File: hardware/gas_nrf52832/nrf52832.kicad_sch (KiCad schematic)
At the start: 15 parts, among them J1 J-link, J4 Conn_01x03, Q3 FDV303N, X1 32.768kHz

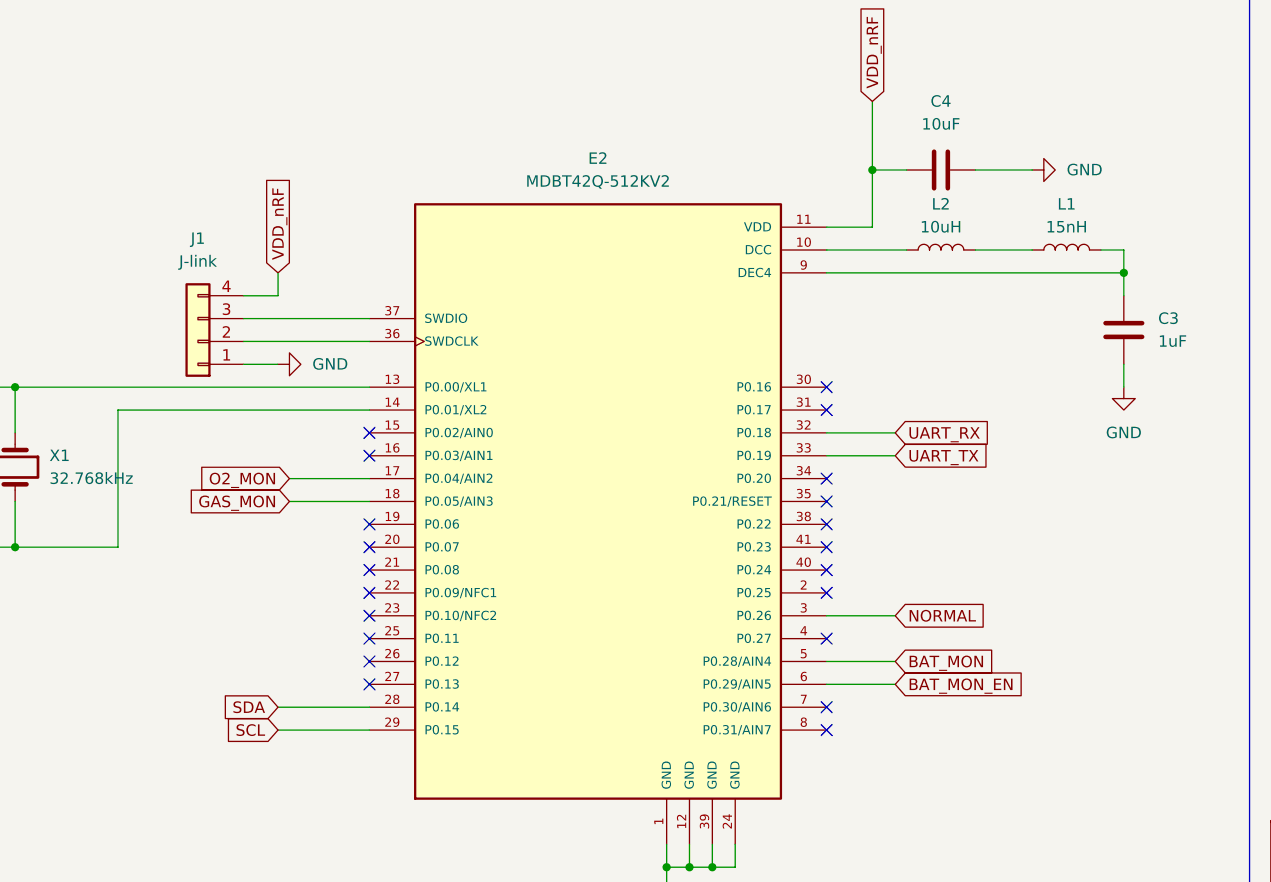
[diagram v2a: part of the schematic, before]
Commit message: test: gas biasing circuit
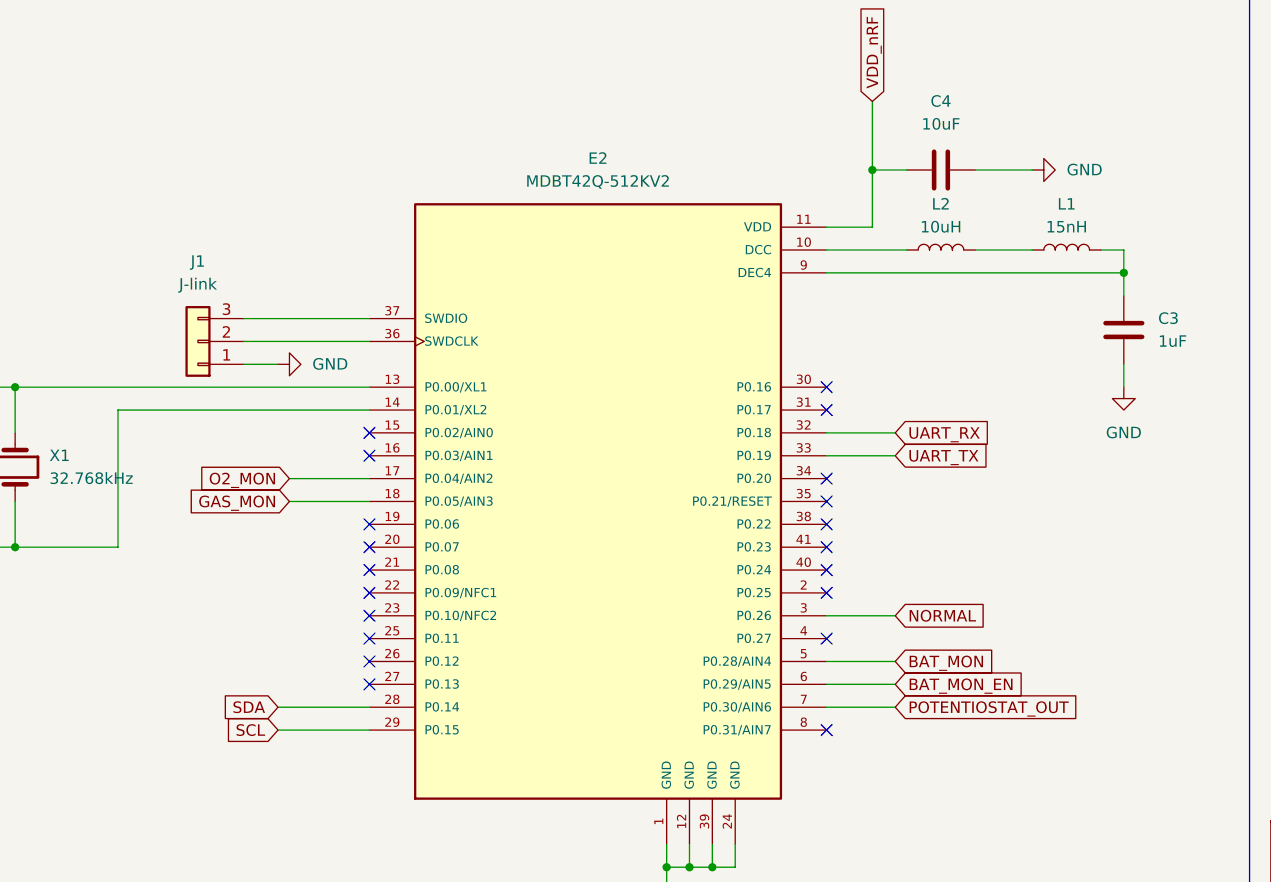
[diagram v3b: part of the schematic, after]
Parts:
- J1: footprint Connector_PinHeader_2.54mm:PinHeader_1x04_P2.54mm_Vertical -> Connector_PinHeader_2.54mm:PinHeader_1x03_P2.54mm_Vertical; symbol Connector_Generic:Conn_01x04 -> Connector_Generic:Conn_01x03; now in the parts list
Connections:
- net VDD_nRF: no longer J1.4 (Pin_4)
- net POTENTIOSTAT_OUT: now reaches E2.7 (P0.30/AIN6)
- no-connect marks 21 -> 20
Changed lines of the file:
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@@
+	)
+	(no_connect
+		(at 77.47 69.85)
 	)
 	(no_connect
@@
 	)
 	(no_connect
-		(at 128.27 97.79)
-	)
-	(no_connect
 		(at 128.27 100.33)
 	)
@@
 		(at 77.47 90.17)
 	)
-	(no_connect
-		(at 77.47 69.85)
-	)
 	(wire
 		(pts
@@
 	(wire
 		(pts
+			(xy 128.27 97.79) (xy 135.89 97.79)
+		)
+		(stroke
+			(width 0)
+			(type default)
+		)
+	)
+	(wire
+		(pts
 			(xy 118.11 115.57) (xy 115.57 115.57)
 		)
@@
 	(wire
 		(pts
-			(xy 67.31 52.07) (xy 63.5 52.07)
-		)
-		(stroke
-			(width 0)
-			(type default)
-		)
-	)
-	(wire
-		(pts
 			(xy 49.53 80.01) (xy 49.53 64.77)
 		)
@@
 			(width 0.1524)
 			(type solid)
-		)
-	)
-	(wire
-		(pts
-			(xy 67.31 49.53) (xy 67.31 52.07)
-		)
-		(stroke
-			(width 0)
-			(type default)
 		)
 	)
@@
 		)
 	)
+	(global_label "POTENTIOSTAT_OUT"
+		(shape input)
+		(at 135.89 97.79 0)
+		(fields_autoplaced yes)
+		(effects
+			(font
+				(size 1.27 1.27)
+			)
+			(justify left)
+		)
+		(property "Intersheetrefs" "${INTERSHEET_REFS}"
+			(at 156.6552 97.79 0)
+			(effects
+				(font
+					(size 1.27 1.27)
+				)
+				(justify left)
+				(hide yes)
+			)
+		)
+	)
 	(global_label "BAT_MON_EN"
 		(shape input)
@@
 				)
 				(justify right)
-				(hide yes)
-			)
-		)
-	)
-	(global_label "VDD_nRF"
-		(shape input)
-		(at 67.31 49.53 90)
-		(fields_autoplaced yes)
-		(effects
-			(font
-				(size 1.27 1.27)
-			)
-			(justify left)
-		)
-		(property "Intersheetrefs" "${INTERSHEET_REFS}"
-			(at 67.31 38.441 90)
-			(effects
-				(font
-					(size 1.27 1.27)
-				)
-				(justify left)
 				(hide yes)
 			)
@@
 	)
 	(symbol
-		(lib_id "Connector_Generic:Conn_01x04")
+		(lib_id "Connector_Generic:Conn_01x03")
 		(at 58.42 57.15 180)
 		(unit 1)
 		(exclude_from_sim no)
-		(in_bom no)
+		(in_bom yes)
 		(on_board yes)
 		(dnp no)
 		(fields_autoplaced yes)
 		(property "Reference" "J1"
-			(at 58.42 45.72 0)
+			(at 58.42 48.26 0)
 			(effects
 				(font
@@
 		)
 		(property "Value" "J-link"
-			(at 58.42 48.26 0)
-			(effects
-				(font
-					(size 1.27 1.27)
-				)
-			)
-		)
-		(property "Footprint" "Connector_PinHeader_2.54mm:PinHeader_1x04_P2.54mm_Vertical"
+			(at 58.42 50.8 0)
+			(effects
+				(font
+					(size 1.27 1.27)
+				)
+			)
+		)
+		(property "Footprint" "Connector_PinHeader_2.54mm:PinHeader_1x03_P2.54mm_Vertical"
 			(at 58.42 57.15 0)
 			(effects
@@
 			)
 		)
-		(property "Description" ""
+		(property "Description" "Generic connector, single row, 01x03, script generated (kicad-library-utils/schlib/autogen/connector/)"
 			(at 58.42 57.15 0)
 			(effects
@@
 		(pin "3"
 		)
-		(pin "4"
-		)
 		(instances

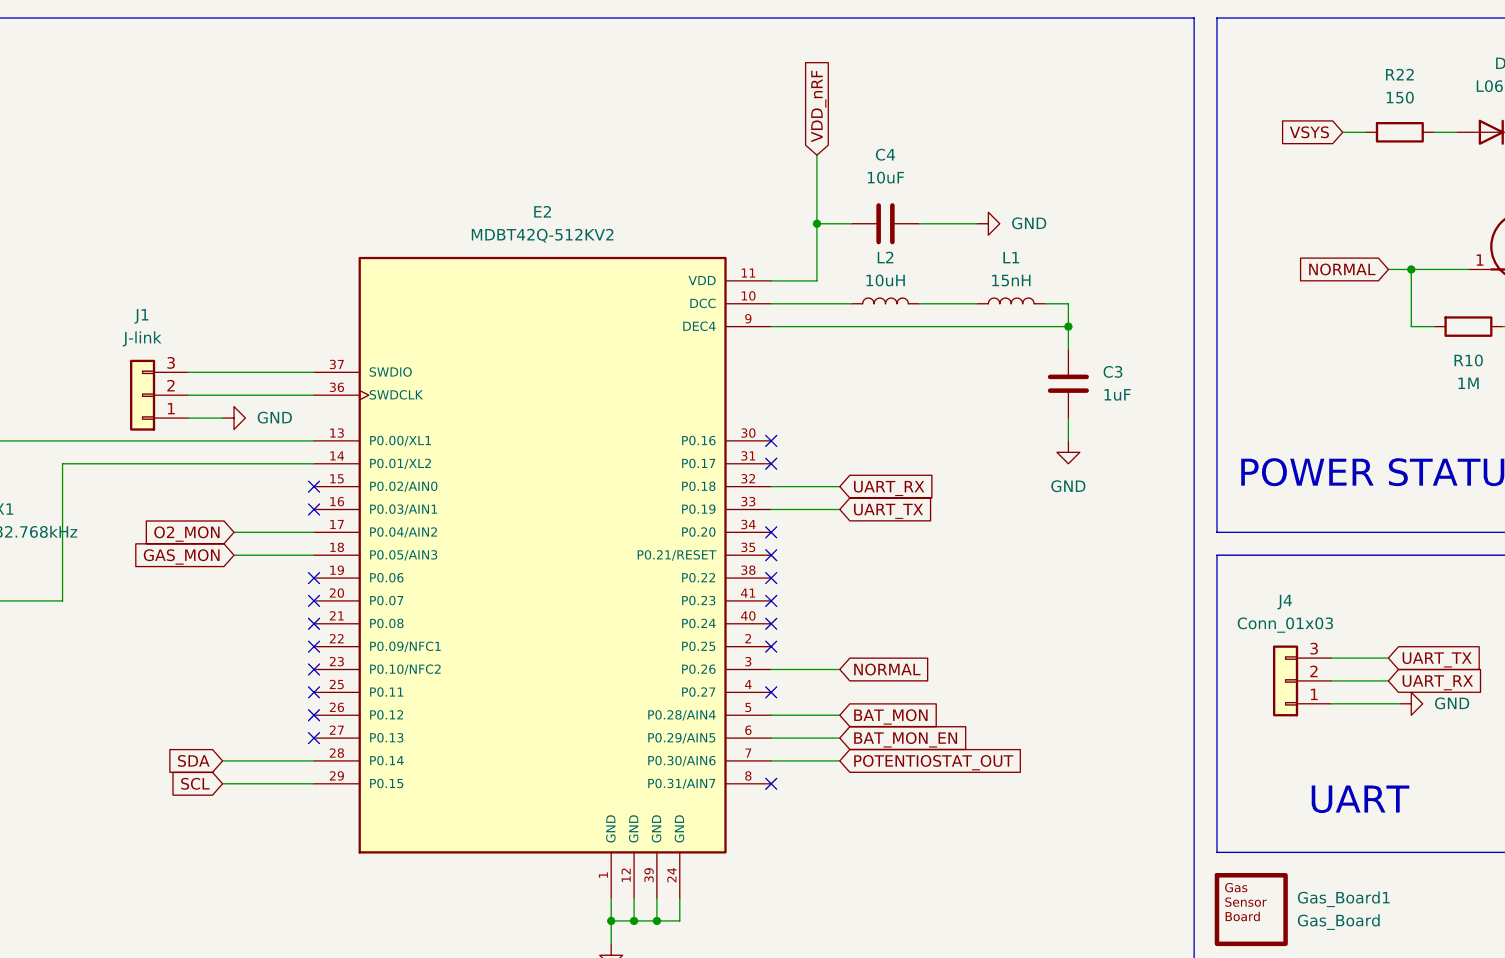
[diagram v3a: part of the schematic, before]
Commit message: feat: hw revision 2.0.1
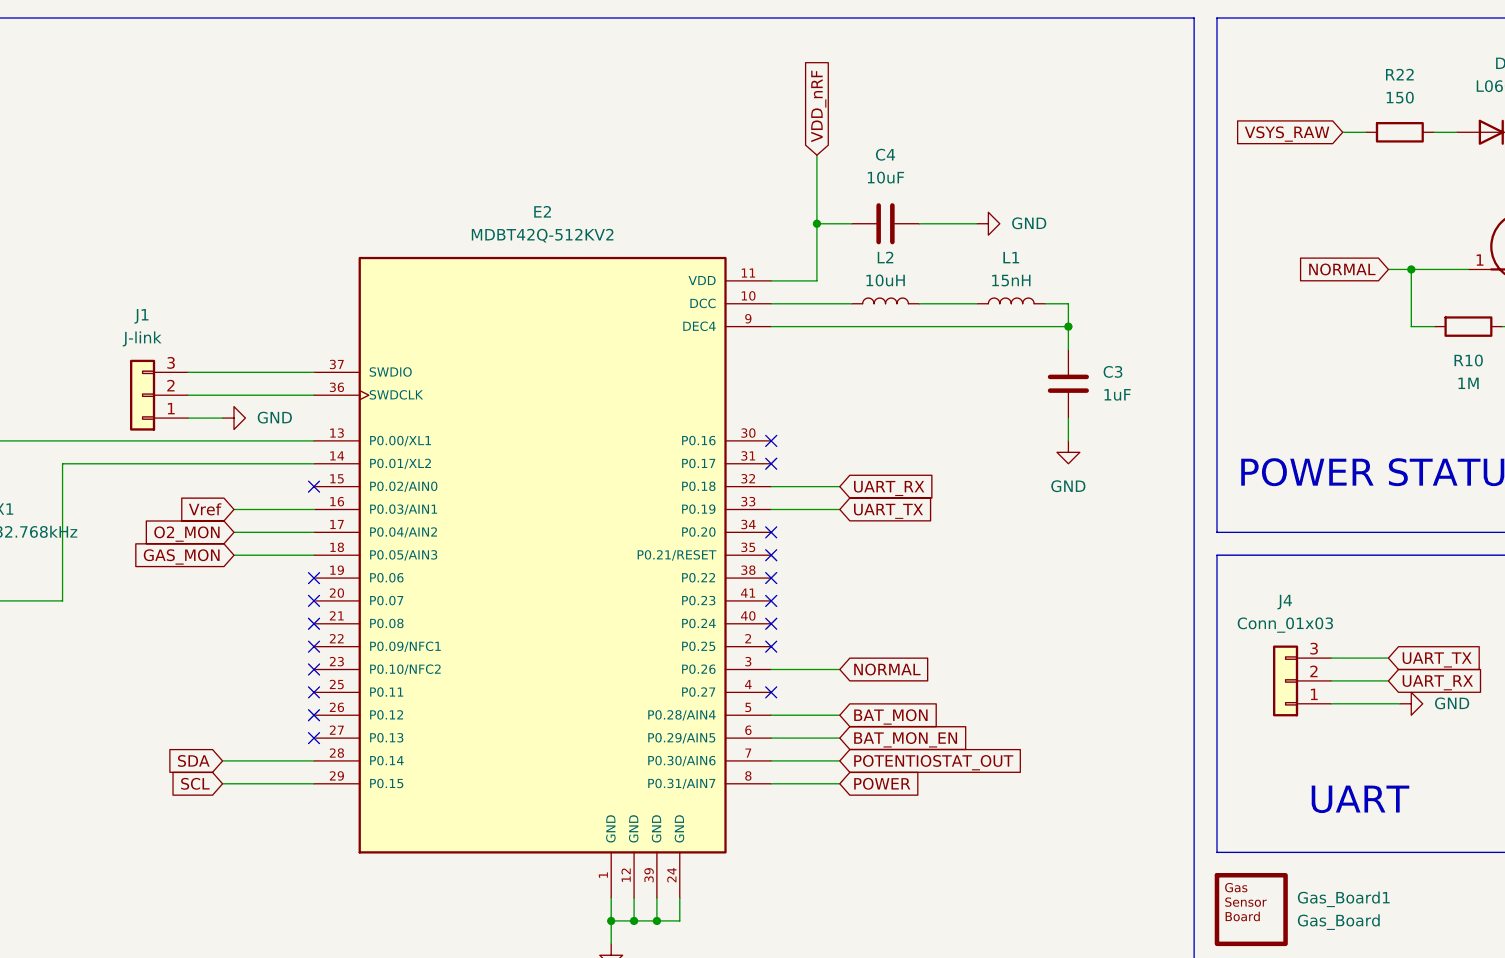
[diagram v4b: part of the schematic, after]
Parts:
- D4: footprint LED_SMD:LED_0603_1608Metric -> WP1533BQ_ID:WP1533BQ; MANUFACTURER BRIGHT LED -> Kingbright; Manufacturer_Part_Number BL-HG036A-AV-TRB -> WP1533BQ/GD; Package 0603 (1608 Metric) -> Tube; Type Surface Mount -> Through Hole; now left out of the parts list
- J1: Type (none) -> Through Hole; now left out of the parts list
- J4: Type (none) -> Through Hole
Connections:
- net Vref: now reaches E2.16 (P0.03/AIN1)
- net POWER: now reaches E2.8 (P0.31/AIN7)
- net VSYS renamed VSYS_RAW
- no-connect marks 20 -> 18
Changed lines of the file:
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@@
-	)
-	(no_connect
-		(at 77.47 69.85)
 	)
 	(no_connect
@@
 	)
 	(no_connect
-		(at 128.27 100.33)
-	)
-	(no_connect
 		(at 128.27 80.01)
 	)
@@
 		(pts
 			(xy 113.03 113.03) (xy 113.03 115.57)
+		)
+		(stroke
+			(width 0)
+			(type default)
+		)
+	)
+	(wire
+		(pts
+			(xy 68.58 69.85) (xy 77.47 69.85)
+		)
+		(stroke
+			(width 0)
+			(type default)
+		)
+	)
+	(wire
+		(pts
+			(xy 128.27 100.33) (xy 135.89 100.33)
 		)
 		(stroke
@@
 		)
 	)
+	(global_label "POWER"
+		(shape input)
+		(at 135.89 100.33 0)
+		(fields_autoplaced yes)
+		(effects
+			(font
+				(size 1.27 1.27)
+			)
+			(justify left)
+		)
+		(property "Intersheetrefs" "${INTERSHEET_REFS}"
+			(at 145.3461 100.33 0)
+			(effects
+				(font
+					(size 1.27 1.27)
+				)
+				(justify left)
+				(hide yes)
+			)
+		)
+	)
 	(global_label "SCL"
 		(shape input)
@@
 		)
 	)
-	(global_label "VSYS"
+	(global_label "VSYS_RAW"
 		(shape input)
 		(at 191.77 27.94 180)
@@
 		)
 		(property "Intersheetrefs" "${INTERSHEET_REFS}"
-			(at 184.1886 27.94 0)
+			(at 179.411 27.94 0)
 			(effects
 				(font
@@
 		(property "Intersheetrefs" "${INTERSHEET_REFS}"
 			(at 56.9467 74.93 0)
+			(effects
+				(font
+					(size 1.27 1.27)
+				)
+				(justify right)
+				(hide yes)
+			)
+		)
+	)
+	(global_label "Vref"
+		(shape input)
+		(at 68.58 69.85 180)
+		(fields_autoplaced yes)
+		(effects
+			(font
+				(size 1.27 1.27)
+			)
+			(justify right)
+		)
+		(property "Intersheetrefs" "${INTERSHEET_REFS}"
+			(at 61.9057 69.85 0)
 			(effects
 				(font
@@
 		(unit 1)
 		(exclude_from_sim no)
-		(in_bom yes)
+		(in_bom no)
 		(on_board yes)
 		(dnp no)
@@
 			)
 		)
-		(property "Footprint" "LED_SMD:LED_0603_1608Metric"
+		(property "Footprint" "WP1533BQ_ID:WP1533BQ"
 			(at 208.28 27.94 0)
 			(effects
@@
 			)
 		)
-		(property "Description" "Yellow Green Light-emitting diode "
+		(property "Description" "LED Circuit Board Indicator Single Green Diffused"
 			(at 208.28 27.94 0)
 			(effects
@@
 			)
 		)
-		(property "Type" "Surface Mount "
+		(property "Type" "Through Hole"
 			(at 208.28 27.94 0)
 			(effects
@@
 			)
 		)
-		(property "Manufacturer_Part_Number" "BL-HG036A-AV-TRB"
+		(property "Manufacturer_Part_Number" "WP1533BQ/GD"
 			(at 208.28 27.94 0)
 			(effects
@@
 			)
 		)
-		(property "MANUFACTURER" "BRIGHT LED"
+		(property "MANUFACTURER" "Kingbright"
 			(at 208.28 27.94 0)
 			(effects
@@
 			)
 		)
-		(property "Package" "0603 (1608 Metric)"
+		(property "Package" "Tube"
 			(at 208.28 27.94 0)
 			(effects
@@
 			)
 		)
-		(property "Type" ""
+		(property "Type" "Through Hole"
 			(at 185.42 88.9 0)
 			(effects
@@
 		(unit 1)
 		(exclude_from_sim no)
-		(in_bom yes)
+		(in_bom no)
 		(on_board yes)
 		(dnp no)
@@
 			)
 		)
-		(property "Type" ""
+		(property "Type" "Through Hole"
 			(at 58.42 57.15 0)
 			(effects
